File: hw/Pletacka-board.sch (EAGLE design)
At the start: 4 parts

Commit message: Add buttons and LEDs
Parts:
- added CON2, CON3, CON4: (no value), #Svorkovnice:AK500/2
- added LED1, LED2, LED3: (no value), led:LEDCHIPLED_0603
- added OK1, OK2, OK3, OK4: PC817, #Optocleny:PC817
- added R1, R5, R7: 1K, rcl_upravena:R-EU_R0603
- added R10, R11, R12, R13, R9: 330R, rcl_upravena:R-EU_R0603
- added R2, R4, R6, R8: 4K7, rcl_upravena:R-EU_R0603
- added S1, S2: (no value), switch-omron:10-XX
- R3: value (none) -> 1K
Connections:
- removed net GPIO12: U$1.12
- removed net GPIO13: U$1.13
- removed net GPIO17: U$1.17
- removed net GPIO21: U$1.21
- removed net GPIO22: U$1.22
- removed net GPIO32: U$1.32
- removed net GPIO36: U$1.36
- removed net GPIO37: U$1.37
- removed net GPIO38: U$1.38
- removed net GPIO39: U$1.39
- new net BUTTON1: R12.2, U$1.13
- new net BUTTON2: R13.2, U$1.12
- new net LED_POWER: R9.2, U$1.21
- new net LED_SEND: R11.2, U$1.17
- new net LED_WIFI: R10.2, U$1.22
- new net N$1: OK1.A, R1.1
- new net N$10: CON4-2.KL, OK4.C
- new net N$11: OK4.A, R7.1
- new net N$12: CON4-1.KL, R7.2
- new net N$13: LED1.A, R9.1
- new net N$14: LED2.A, R10.1
- new net N$15: LED3.A, R11.1
- new net N$16: R12.1, S1.P, S1.P1
- new net N$17: R13.1, S2.P, S2.P1
- new net N$2: CON1-2.KL, OK1.C
- new net N$3: CON2-2.KL, OK2.C
- new net N$4: CON1-1.KL, R1.2
- new net N$5: OK2.A, R3.1
- new net N$6: CON2-1.KL, R3.2
- new net N$7: CON3-2.KL, OK3.C
- new net N$8: OK3.A, R5.1
- new net N$9: CON3-1.KL, R5.2
- new net OPTO1: OK1.COL, R2.2, U$1.36
- new net OPTO2: OK2.COL, R4.2, U$1.37
- new net OPTO3: OK3.COL, R6.2, U$1.38
- new net OPTO4: OK4.COL, R8.2, U$1.39
- new net RFID: RDM1.RX, U$1.32
- net +3V3: now also R2.1, R4.1, R6.1, R8.1
- net +5V: now also RDM1.VCC
- net GND: now also LED1.C, LED2.C, LED3.C, OK1.EMIT, OK2.EMIT, OK3.EMIT, OK4.EMIT, RDM1.GND, S1.S, S1.S1, S2.S, S2.S1
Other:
- note added: "1"
- note added: "2"
- note added: "3"
- note added: "4"
- note added: "Optocoplers"

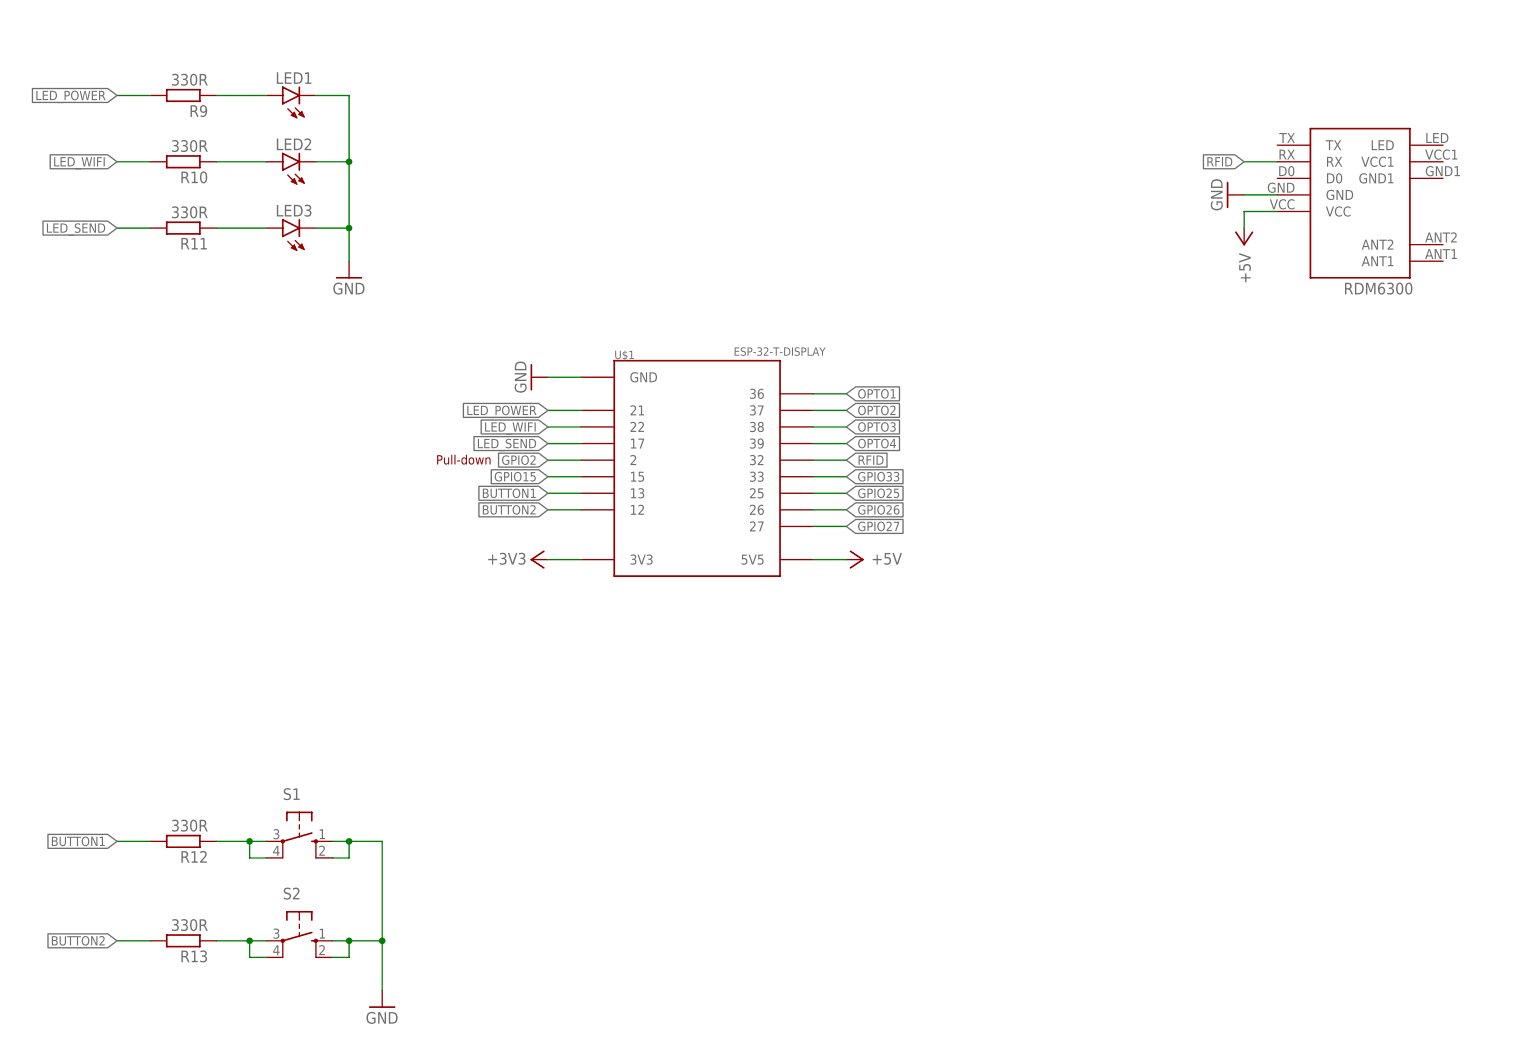
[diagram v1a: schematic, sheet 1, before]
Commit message: Add temperature sensor
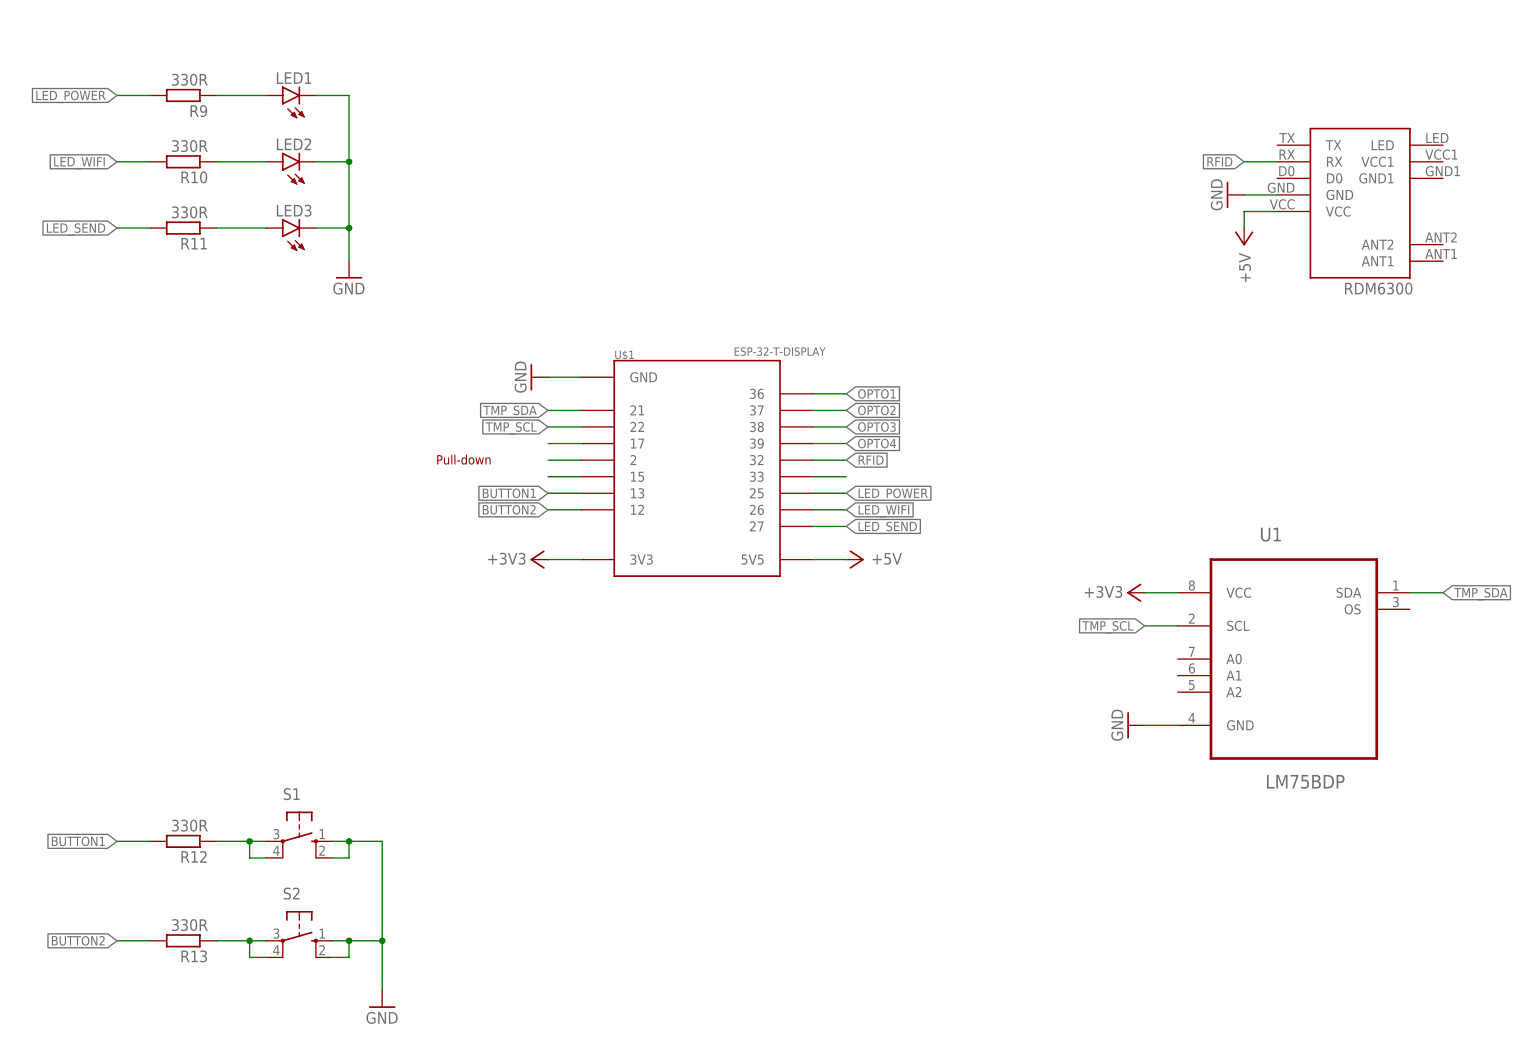
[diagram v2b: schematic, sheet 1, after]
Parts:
- added U1: LM75BDP, LM75BDP:LM75BDP
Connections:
- removed net GPIO25: U$1.25
- removed net GPIO26: U$1.26
- removed net GPIO27: U$1.27
- new net N$20: U$1.17
- new net TMP_SCL: U$1.22, U1.SCL
- new net TMP_SDA: U$1.21, U1.SDA
- net +3V3: now also U1.VCC
- net GND: now also U1.GND
- net LED_POWER: now also U$1.25; no longer U$1.21
- net LED_SEND: now also U$1.27; no longer U$1.17
- net LED_WIFI: now also U$1.26; no longer U$1.22
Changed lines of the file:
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@@
 <part name="GND8" library="supply1" library_urn="urn:adsk.eagle:library:371" deviceset="GND" device=""/>
 <part name="R13" library="rcl_upravena" deviceset="R-EU_" device="R0603" value="330R"/>
+<part name="U1" library="LM75BDP" deviceset="LM75BDP" device=""/>
+<part name="GND9" library="supply1" library_urn="urn:adsk.eagle:library:371" deviceset="GND" device=""/>
+<part name="+3V6" library="supply1" library_urn="urn:adsk.eagle:library:371" deviceset="+3V3" device=""/>
 </parts>
 <sheets>
@@
 <attribute name="VALUE" x="41.91" y="28.702" size="1.778" layer="96" rot="R180"/>
 </instance>
+<instance part="U1" gate="A" x="208.28" y="71.12" smashed="yes">
+<attribute name="NAME" x="203.012159375" y="86.6181" size="2.08678125" layer="95" ratio="10" rot="SR0"/>
+<attribute name="VALUE" x="203.90995" y="48.7362" size="2.083390625" layer="96" ratio="10" rot="SR0"/>
+</instance>
+<instance part="GND9" gate="1" x="182.88" y="58.42" smashed="yes" rot="R270">
+<attribute name="VALUE" x="180.34" y="60.96" size="1.778" layer="96" rot="R270"/>
+</instance>
+<instance part="+3V6" gate="G$1" x="182.88" y="78.74" smashed="yes" rot="R90">
+<attribute name="VALUE" x="176.022" y="77.978" size="1.778" layer="96"/>
+</instance>
 </instances>
 <busses>
@@
 <net name="LED_POWER" class="0">
 <segment>
-<pinref part="U$1" gate="G$1" pin="21"/>
-<wire x1="99.06" y1="106.68" x2="93.98" y2="106.68" width="0.1524" layer="91"/>
-<label x="93.98" y="106.68" size="1.4224" layer="95" rot="R180" xref="yes"/>
-</segment>
-<segment>
 <pinref part="R9" gate="G$1" pin="2"/>
 <wire x1="33.02" y1="154.94" x2="27.94" y2="154.94" width="0.1524" layer="91"/>
 <label x="27.94" y="154.94" size="1.4224" layer="95" ratio="20" rot="R180" xref="yes"/>
 </segment>
+<segment>
+<pinref part="U$1" gate="G$1" pin="25"/>
+<wire x1="134.62" y1="93.98" x2="139.7" y2="93.98" width="0.1524" layer="91"/>
+<label x="139.7" y="93.98" size="1.4224" layer="95" xref="yes"/>
+</segment>
 </net>
 <net name="OPTO1" class="0">
@@
 <pinref part="U$1" gate="G$1" pin="33"/>
 <wire x1="134.62" y1="96.52" x2="139.7" y2="96.52" width="0.1524" layer="91"/>
-<label x="139.7" y="96.52" size="1.4224" layer="95" xref="yes"/>
-</segment>
-</net>
-<net name="GPIO25" class="0">
-<segment>
-<pinref part="U$1" gate="G$1" pin="25"/>
-<wire x1="134.62" y1="93.98" x2="139.7" y2="93.98" width="0.1524" layer="91"/>
-<label x="139.7" y="93.98" size="1.4224" layer="95" xref="yes"/>
-</segment>
-</net>
-<net name="GPIO26" class="0">
-<segment>
-<pinref part="U$1" gate="G$1" pin="26"/>
-<wire x1="134.62" y1="91.44" x2="139.7" y2="91.44" width="0.1524" layer="91"/>
-<label x="139.7" y="91.44" size="1.4224" layer="95" xref="yes"/>
-</segment>
-</net>
-<net name="GPIO27" class="0">
+</segment>
+</net>
+<net name="BUTTON2" class="0">
+<segment>
+<pinref part="U$1" gate="G$1" pin="12"/>
+<wire x1="99.06" y1="91.44" x2="93.98" y2="91.44" width="0.1524" layer="91"/>
+<label x="93.98" y="91.44" size="1.4224" layer="95" rot="R180" xref="yes"/>
+</segment>
+<segment>
+<pinref part="R13" gate="G$1" pin="2"/>
+<wire x1="33.02" y1="25.4" x2="27.94" y2="25.4" width="0.1524" layer="91"/>
+<label x="27.94" y="25.4" size="1.4224" layer="95" ratio="20" rot="R180" xref="yes"/>
+</segment>
+</net>
+<net name="BUTTON1" class="0">
+<segment>
+<pinref part="U$1" gate="G$1" pin="13"/>
+<wire x1="99.06" y1="93.98" x2="93.98" y2="93.98" width="0.1524" layer="91"/>
+<label x="93.98" y="93.98" size="1.4224" layer="95" rot="R180" xref="yes"/>
+</segment>
+<segment>
+<pinref part="R12" gate="G$1" pin="2"/>
+<wire x1="33.02" y1="40.64" x2="27.94" y2="40.64" width="0.1524" layer="91"/>
+<label x="27.94" y="40.64" size="1.4224" layer="95" ratio="20" rot="R180" xref="yes"/>
+</segment>
+</net>
+<net name="GPIO15" class="0">
+<segment>
+<pinref part="U$1" gate="G$1" pin="15"/>
+<wire x1="99.06" y1="96.52" x2="93.98" y2="96.52" width="0.1524" layer="91"/>
+</segment>
+</net>
+<net name="GPIO2" class="0">
+<segment>
+<pinref part="U$1" gate="G$1" pin="2"/>
+<wire x1="99.06" y1="99.06" x2="93.98" y2="99.06" width="0.1524" layer="91"/>
+</segment>
+</net>
+<net name="LED_SEND" class="0">
+<segment>
+<pinref part="R11" gate="G$1" pin="2"/>
+<wire x1="33.02" y1="134.62" x2="27.94" y2="134.62" width="0.1524" layer="91"/>
+<label x="27.94" y="134.62" size="1.4224" layer="95" ratio="20" rot="R180" xref="yes"/>
+</segment>
 <segment>
 <pinref part="U$1" gate="G$1" pin="27"/>
@@
 </segment>
 </net>
-<net name="BUTTON2" class="0">
-<segment>
-<pinref part="U$1" gate="G$1" pin="12"/>
-<wire x1="99.06" y1="91.44" x2="93.98" y2="91.44" width="0.1524" layer="91"/>
-<label x="93.98" y="91.44" size="1.4224" layer="95" rot="R180" xref="yes"/>
-</segment>
-<segment>
-<pinref part="R13" gate="G$1" pin="2"/>
-<wire x1="33.02" y1="25.4" x2="27.94" y2="25.4" width="0.1524" layer="91"/>
-<label x="27.94" y="25.4" size="1.4224" layer="95" ratio="20" rot="R180" xref="yes"/>
-</segment>
-</net>
-<net name="BUTTON1" class="0">
-<segment>
-<pinref part="U$1" gate="G$1" pin="13"/>
-<wire x1="99.06" y1="93.98" x2="93.98" y2="93.98" width="0.1524" layer="91"/>
-<label x="93.98" y="93.98" size="1.4224" layer="95" rot="R180" xref="yes"/>
-</segment>
-<segment>
-<pinref part="R12" gate="G$1" pin="2"/>
-<wire x1="33.02" y1="40.64" x2="27.94" y2="40.64" width="0.1524" layer="91"/>
-<label x="27.94" y="40.64" size="1.4224" layer="95" ratio="20" rot="R180" xref="yes"/>
-</segment>
-</net>
-<net name="GPIO15" class="0">
-<segment>
-<pinref part="U$1" gate="G$1" pin="15"/>
-<wire x1="99.06" y1="96.52" x2="93.98" y2="96.52" width="0.1524" layer="91"/>
-<label x="93.98" y="96.52" size="1.4224" layer="95" rot="R180" xref="yes"/>
-</segment>
-</net>
-<net name="GPIO2" class="0">
-<segment>
-<pinref part="U$1" gate="G$1" pin="2"/>
-<wire x1="99.06" y1="99.06" x2="93.98" y2="99.06" width="0.1524" layer="91"/>
-<label x="93.98" y="99.06" size="1.4224" layer="95" rot="R180" xref="yes"/>
-</segment>
-</net>
-<net name="LED_SEND" class="0">
-<segment>
-<pinref part="U$1" gate="G$1" pin="17"/>
-<wire x1="99.06" y1="101.6" x2="93.98" y2="101.6" width="0.1524" layer="91"/>
-<label x="93.98" y="101.6" size="1.4224" layer="95" rot="R180" xref="yes"/>
-</segment>
-<segment>
-<pinref part="R11" gate="G$1" pin="2"/>
-<wire x1="33.02" y1="134.62" x2="27.94" y2="134.62" width="0.1524" layer="91"/>
-<label x="27.94" y="134.62" size="1.4224" layer="95" ratio="20" rot="R180" xref="yes"/>
-</segment>
-</net>
 <net name="+3V3" class="0">
 <segment>
@@
 <wire x1="93.98" y1="83.82" x2="99.06" y2="83.82" width="0.1524" layer="91"/>
 <pinref part="+3V2" gate="G$1" pin="+3V3"/>
+</segment>
+<segment>
+<pinref part="+3V6" gate="G$1" pin="+3V3"/>
+<pinref part="U1" gate="A" pin="VCC"/>
+<wire x1="185.42" y1="78.74" x2="190.5" y2="78.74" width="0.1524" layer="91"/>
 </segment>
 </net>
@@
 <pinref part="GND8" gate="1" pin="GND"/>
 </segment>
+<segment>
+<pinref part="GND9" gate="1" pin="GND"/>
+<pinref part="U1" gate="A" pin="GND"/>
+<wire x1="185.42" y1="58.42" x2="190.5" y2="58.42" width="0.1524" layer="91"/>
+</segment>
 </net>
 <net name="OPTO2" class="0">
@@
 </segment>
 <segment>
-<pinref part="U$1" gate="G$1" pin="22"/>
-<wire x1="99.06" y1="104.14" x2="93.98" y2="104.14" width="0.1524" layer="91"/>
-<label x="93.98" y="104.14" size="1.4224" layer="95" rot="R180" xref="yes"/>
+<pinref part="U$1" gate="G$1" pin="26"/>
+<wire x1="134.62" y1="91.44" x2="139.7" y2="91.44" width="0.1524" layer="91"/>
+<label x="139.7" y="91.44" size="1.4224" layer="95" xref="yes"/>
 </segment>
 </net>
@@
 </segment>
 </net>
+<net name="TMP_SDA" class="0">
+<segment>
+<pinref part="U$1" gate="G$1" pin="21"/>
+<wire x1="99.06" y1="106.68" x2="93.98" y2="106.68" width="0.1524" layer="91"/>
+<label x="93.98" y="106.68" size="1.4224" layer="95" ratio="20" rot="R180" xref="yes"/>
+</segment>
+<segment>
+<pinref part="U1" gate="A" pin="SDA"/>
+<wire x1="226.06" y1="78.74" x2="231.14" y2="78.74" width="0.1524" layer="91"/>
+<label x="231.14" y="78.74" size="1.4224" layer="95" ratio="20" xref="yes"/>
+</segment>
+</net>
+<net name="TMP_SCL" class="0">
+<segment>
+<pinref part="U$1" gate="G$1" pin="22"/>
+<wire x1="99.06" y1="104.14" x2="93.98" y2="104.14" width="0.1524" layer="91"/>
+<label x="93.98" y="104.14" size="1.4224" layer="95" ratio="20" rot="R180" xref="yes"/>
+</segment>
+<segment>
+<pinref part="U1" gate="A" pin="SCL"/>
+<wire x1="190.5" y1="73.66" x2="185.42" y2="73.66" width="0.1524" layer="91"/>
+<label x="185.42" y="73.66" size="1.4224" layer="95" ratio="20" rot="R180" xref="yes"/>
+</segment>
+</net>
+<net name="N$20" class="0">
+<segment>
+<pinref part="U$1" gate="G$1" pin="17"/>
+<wire x1="99.06" y1="101.6" x2="93.98" y2="101.6" width="0.1524" layer="91"/>
+</segment>
+</net>

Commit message: Start routing
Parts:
- renumbered CON1 to OPTO1
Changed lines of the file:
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@@
 <part name="FRAME2" library="frames" library_urn="urn:adsk.eagle:library:229" deviceset="A4L-LOC" device=""/>
 <part name="U$1" library="ESP32-T-Display" deviceset="ESP-32-T-DISPLAY" device=""/>
-<part name="CON1" library="#Svorkovnice" deviceset="AK500/2" device=""/>
+<part name="OPTO1" library="#Svorkovnice" deviceset="AK500/2" device=""/>
 <part name="RDM1" library="RDM6300" deviceset="RDM6300" device=""/>
 <part name="+3V2" library="supply1" library_urn="urn:adsk.eagle:library:371" deviceset="+3V3" device=""/>
@@
 <attribute name="SHEET" x="230.505" y="5.08" size="2.54" layer="94"/>
 </instance>
-<instance part="CON1" gate="-1" x="27.94" y="142.24" smashed="yes">
+<instance part="OPTO1" gate="-1" x="27.94" y="142.24" smashed="yes">
 <attribute name="NAME" x="26.67" y="143.129" size="1.778" layer="95" rot="R180"/>
 </instance>
-<instance part="CON1" gate="-2" x="27.94" y="137.16" smashed="yes">
+<instance part="OPTO1" gate="-2" x="27.94" y="137.16" smashed="yes">
 <attribute name="NAME" x="26.67" y="138.049" size="1.778" layer="95" rot="R180"/>
 <attribute name="VALUE" x="24.13" y="133.477" size="1.778" layer="96"/>
@@
 <net name="N$2" class="0">
 <segment>
-<pinref part="CON1" gate="-2" pin="KL"/>
+<pinref part="OPTO1" gate="-2" pin="KL"/>
 <pinref part="OK1" gate="A" pin="C"/>
 <wire x1="33.02" y1="137.16" x2="48.26" y2="137.16" width="0.1524" layer="91"/>
@@
 <net name="N$4" class="0">
 <segment>
-<pinref part="CON1" gate="-1" pin="KL"/>
+<pinref part="OPTO1" gate="-1" pin="KL"/>
 <pinref part="R1" gate="G$1" pin="2"/>
 <wire x1="33.02" y1="142.24" x2="35.56" y2="142.24" width="0.1524" layer="91"/>
